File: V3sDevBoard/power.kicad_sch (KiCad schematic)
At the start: 48 parts, among them J10 Power, U2 SY8089AAAC, U3 SY8089AAAC, U4 SY8089AAAC, U6 PT4103

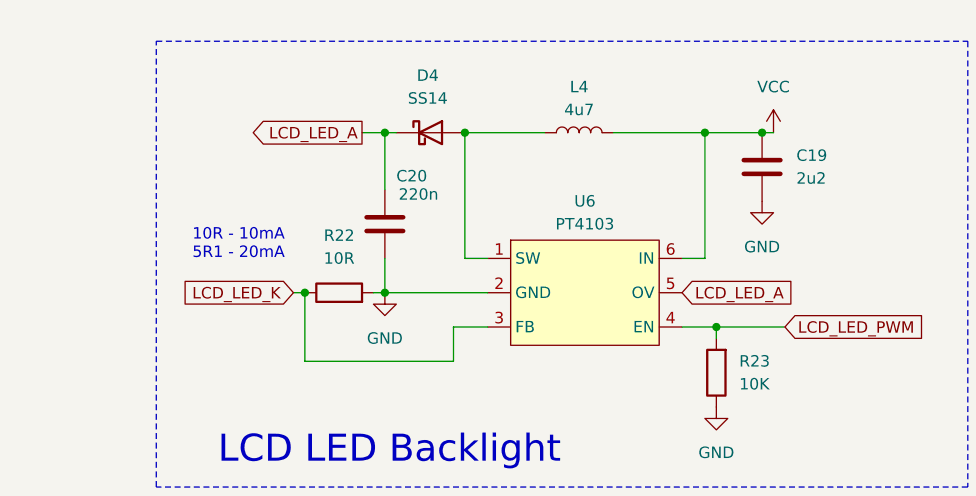
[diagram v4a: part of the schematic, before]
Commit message: first attempts to arrange components on a PCB
plus making footprints bme280&mpu6050 easier to hand solder.
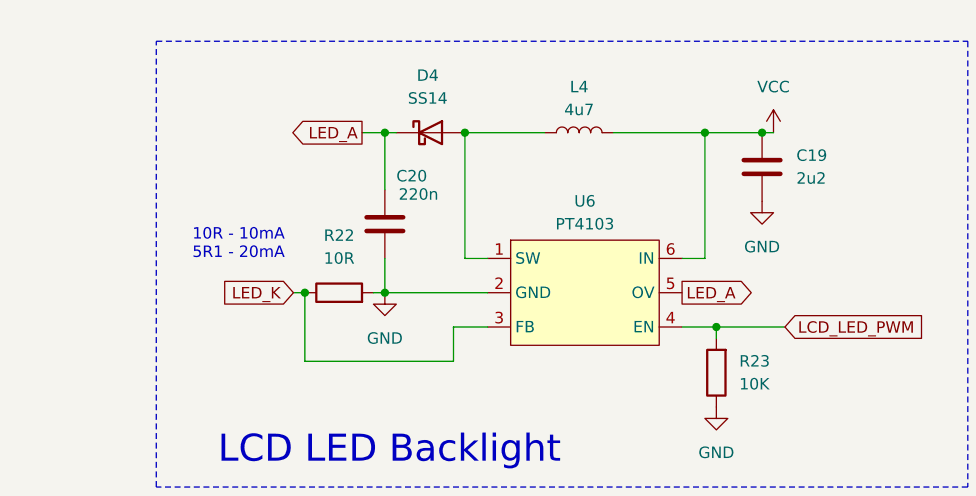
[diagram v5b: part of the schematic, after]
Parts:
- L1, L2, L3, L4: footprint Inductor_SMD:L_APV_APH0420 -> Inductor_SMD:L_APV_APH0420_HandSolder
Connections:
- net LCD_LED_A renamed LED_A
- net LCD_LED_K renamed LED_K
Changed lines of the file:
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@@
 		)
 	)
-	(global_label "LCD_LED_A"
+	(global_label "LED_A"
 		(shape output)
 		(at 194.31 27.94 180)
@@
 		)
 		(property "Intersheetrefs" "${INTERSHEET_REFS}"
-			(at 181.2858 27.94 0)
+			(at 185.8215 27.94 0)
 			(effects
 				(font
@@
 		)
 	)
-	(global_label "RGB"
-		(shape input)
-		(at 175.26 92.71 180)
+	(global_label "LED_A"
+		(shape output)
+		(at 229.87 45.72 0)
 		(fields_autoplaced yes)
 		(effects
@@
 				(size 1.27 1.27)
 			)
-			(justify right)
+			(justify left)
 		)
 		(property "Intersheetrefs" "${INTERSHEET_REFS}"
-			(at 168.4648 92.71 0)
+			(at 238.3585 45.72 0)
 			(effects
 				(font
 					(size 1.27 1.27)
 				)
-				(justify right)
+				(justify left)
 				(hide yes)
 			)
 		)
 	)
-	(global_label "LCD_LED_A"
+	(global_label "RGB"
 		(shape input)
-		(at 229.87 45.72 0)
+		(at 175.26 92.71 180)
 		(fields_autoplaced yes)
 		(effects
@@
 				(size 1.27 1.27)
 			)
-			(justify left)
+			(justify right)
 		)
 		(property "Intersheetrefs" "${INTERSHEET_REFS}"
-			(at 242.8942 45.72 0)
+			(at 168.4648 92.71 0)
 			(effects
 				(font
 					(size 1.27 1.27)
 				)
-				(justify left)
+				(justify right)
 				(hide yes)
 			)
 		)
 	)
-	(global_label "LCD_LED_K"
+	(global_label "LED_K"
 		(shape input)
 		(at 186.69 45.72 180)
@@
 		)
 		(property "Intersheetrefs" "${INTERSHEET_REFS}"
-			(at 173.4844 45.72 0)
+			(at 178.0201 45.72 0)
 			(effects
 				(font
@@
 		)
 	)
+	(rule_area
+		(polyline
+			(pts
+				(xy 36.83 21.59) (xy 36.83 58.42) (xy 39.37 60.96) (xy 73.66 60.96) (xy 73.66 69.85) (xy 119.38 69.85)
+				(xy 119.38 69.215) (xy 119.38 39.37) (xy 92.71 39.37) (xy 91.44 40.64) (xy 91.44 17.78) (xy 40.64 17.78)
+			)
+			(stroke
+				(width 0)
+				(type dash)
+			)
+			(fill
+				(type none)
+			)
+		)
+	)
+	(rule_area
+		(polyline
+			(pts
+				(xy 35.56 71.12) (xy 35.56 105.41) (xy 36.83 106.68) (xy 74.93 106.68) (xy 74.93 118.11) (xy 77.47 120.65)
+				(xy 127 120.65) (xy 127 88.9) (xy 124.46 86.36) (xy 92.71 86.36) (xy 90.17 83.82) (xy 90.17 76.2)
+				(xy 76.2 76.2) (xy 71.12 71.12) (xy 71.12 64.77) (xy 41.91 64.77)
+			)
+			(stroke
+				(width 0)
+				(type dash)
+			)
+			(fill
+				(type none)
+			)
+		)
+	)
+	(rule_area
+		(polyline
+			(pts
+				(xy 35.56 119.38) (xy 35.56 154.94) (xy 49.53 168.91) (xy 127 168.91) (xy 128.27 167.64) (xy 128.27 133.35)
+				(xy 119.38 124.46) (xy 76.2 124.46) (xy 72.39 120.65) (xy 72.39 114.3) (xy 40.64 114.3)
+			)
+			(stroke
+				(width 0)
+				(type dash)
+			)
+			(fill
+				(type none)
+			)
+		)
+	)
 	(netclass_flag ""
 		(length 2.54)
@@
 		(length 2.54)
 		(shape round)
+		(at 119.38 39.37 0)
+		(fields_autoplaced yes)
+		(effects
+			(font
+				(size 1.27 1.27)
+			)
+			(justify left bottom)
+		)
+		(property "Netclass" ""
+			(at 120.0785 36.83 0)
+			(effects
+				(font
+					(size 1.27 1.27)
+				)
+				(justify left)
+			)
+		)
+		(property "Component Class" "3V3 Power"
+			(at 120.0785 36.83 0)
+			(effects
+				(font
+					(size 1.27 1.27)
+					(italic yes)
+				)
+				(justify left)
+			)
+		)
+	)
+	(netclass_flag ""
+		(length 2.54)
+		(shape round)
 		(at 115.57 99.06 0)
 		(effects
@@
 		(length 2.54)
 		(shape round)
+		(at 120.65 86.36 0)
+		(fields_autoplaced yes)
+		(effects
+			(font
+				(size 1.27 1.27)
+			)
+			(justify left bottom)
+		)
+		(property "Netclass" ""
+			(at 121.3485 83.82 0)
+			(effects
+				(font
+					(size 1.27 1.27)
+				)
+				(justify left)
+			)
+		)
+		(property "Component Class" "1V8 Power"
+			(at 121.3485 83.82 0)
+			(effects
+				(font
+					(size 1.27 1.27)
+					(italic yes)
+				)
+				(justify left)
+			)
+		)
+	)
+	(netclass_flag ""
+		(length 2.54)
+		(shape round)
+		(at 128.27 133.35 0)
+		(fields_autoplaced yes)
+		(effects
+			(font
+				(size 1.27 1.27)
+			)
+			(justify left bottom)
+		)
+		(property "Netclass" ""
+			(at 128.9685 130.81 0)
+			(effects
+				(font
+					(size 1.27 1.27)
+				)
+				(justify left)
+			)
+		)
+		(property "Component Class" "1V2 Power"
+			(at 128.9685 130.81 0)
+			(effects
+				(font
+					(size 1.27 1.27)
+					(italic yes)
+				)
+				(justify left)
+			)
+		)
+	)
+	(netclass_flag ""
+		(length 2.54)
+		(shape round)
 		(at 67.31 22.86 90)
 		(effects
@@
 			)
 		)
-		(property "Footprint" "Inductor_SMD:L_APV_APH0420"
+		(property "Footprint" "Inductor_SMD:L_APV_APH0420_HandSolder"
 			(at 218.44 27.94 0)
 			(effects
@@
 			)
 		)
-		(property "Footprint" "Inductor_SMD:L_APV_APH0420"
+		(property "Footprint" "Inductor_SMD:L_APV_APH0420_HandSolder"
 			(at 86.36 148.59 0)
 			(effects
@@
 			)
 		)
-		(property "Footprint" "Inductor_SMD:L_APV_APH0420"
+		(property "Footprint" "Inductor_SMD:L_APV_APH0420_HandSolder"
 			(at 86.36 49.53 0)
 			(effects
@@
 			)
 		)
-		(property "Footprint" "Inductor_SMD:L_APV_APH0420"
+		(property "Footprint" "Inductor_SMD:L_APV_APH0420_HandSolder"
 			(at 86.36 99.06 0)
 			(effects

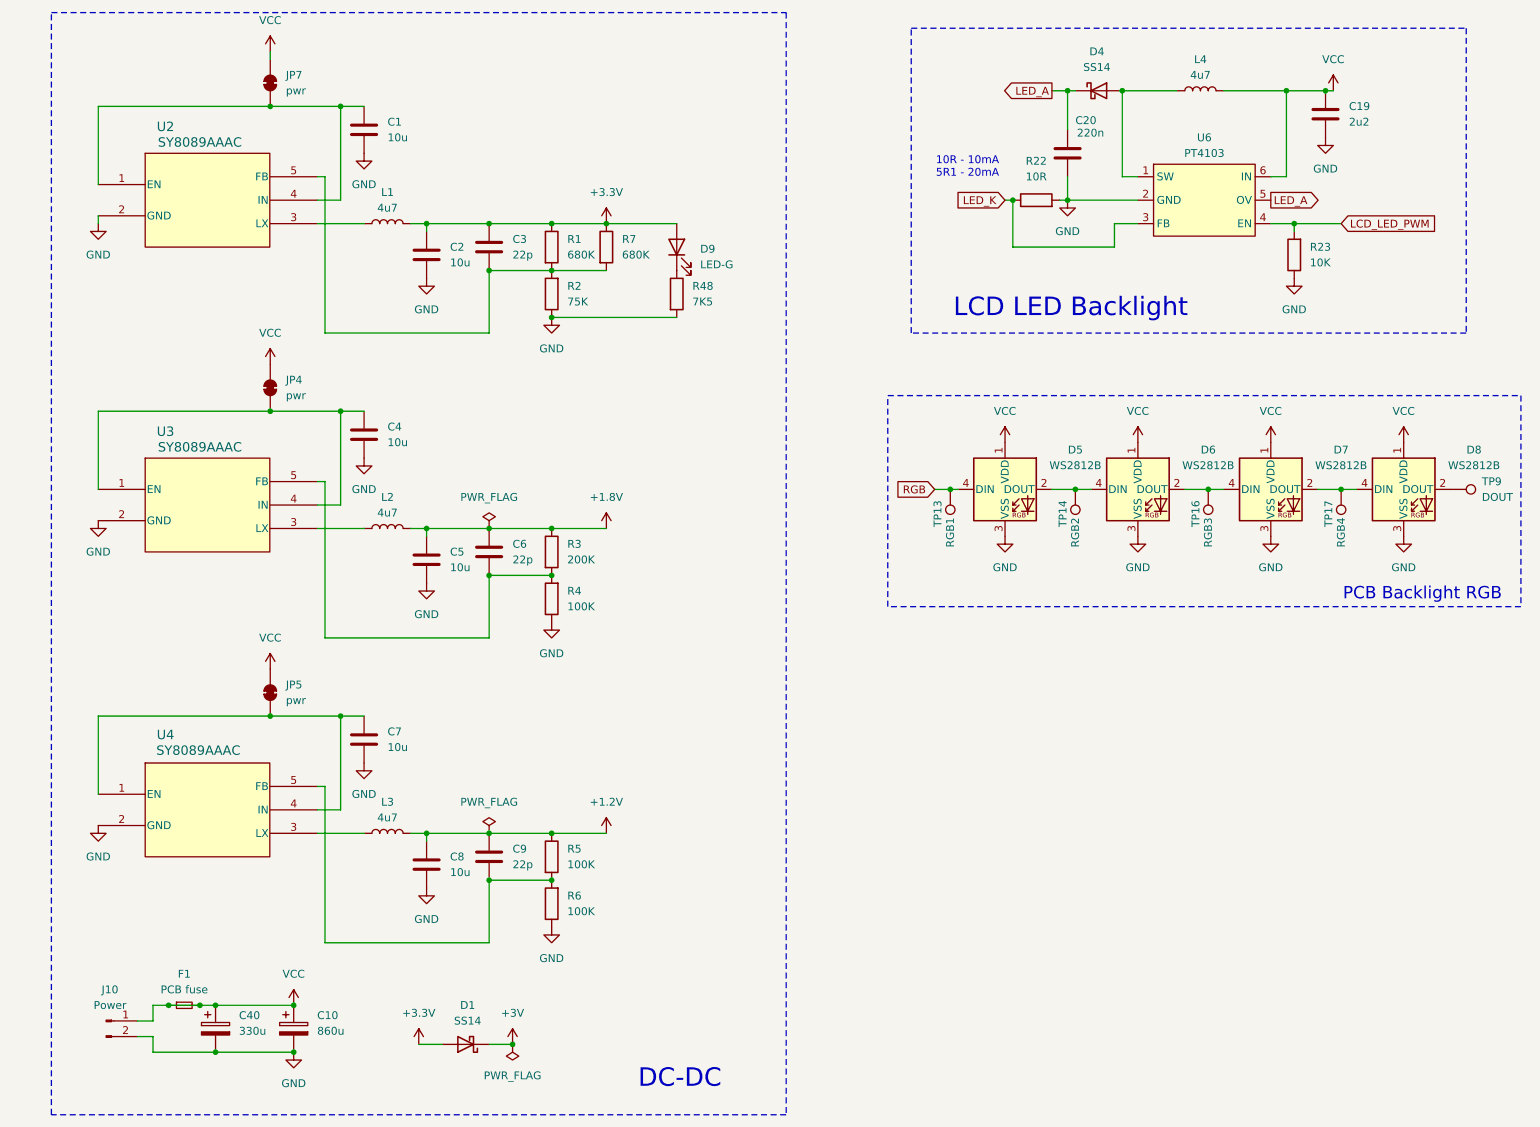
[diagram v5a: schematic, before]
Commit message: completing pcb desgin
Returning to project after month away. Switching to 4-layer desgin on 3313 stackup sig-gnd-pow-sig, changing size of some passive to 0603, connecting all components, adding silkscreen.
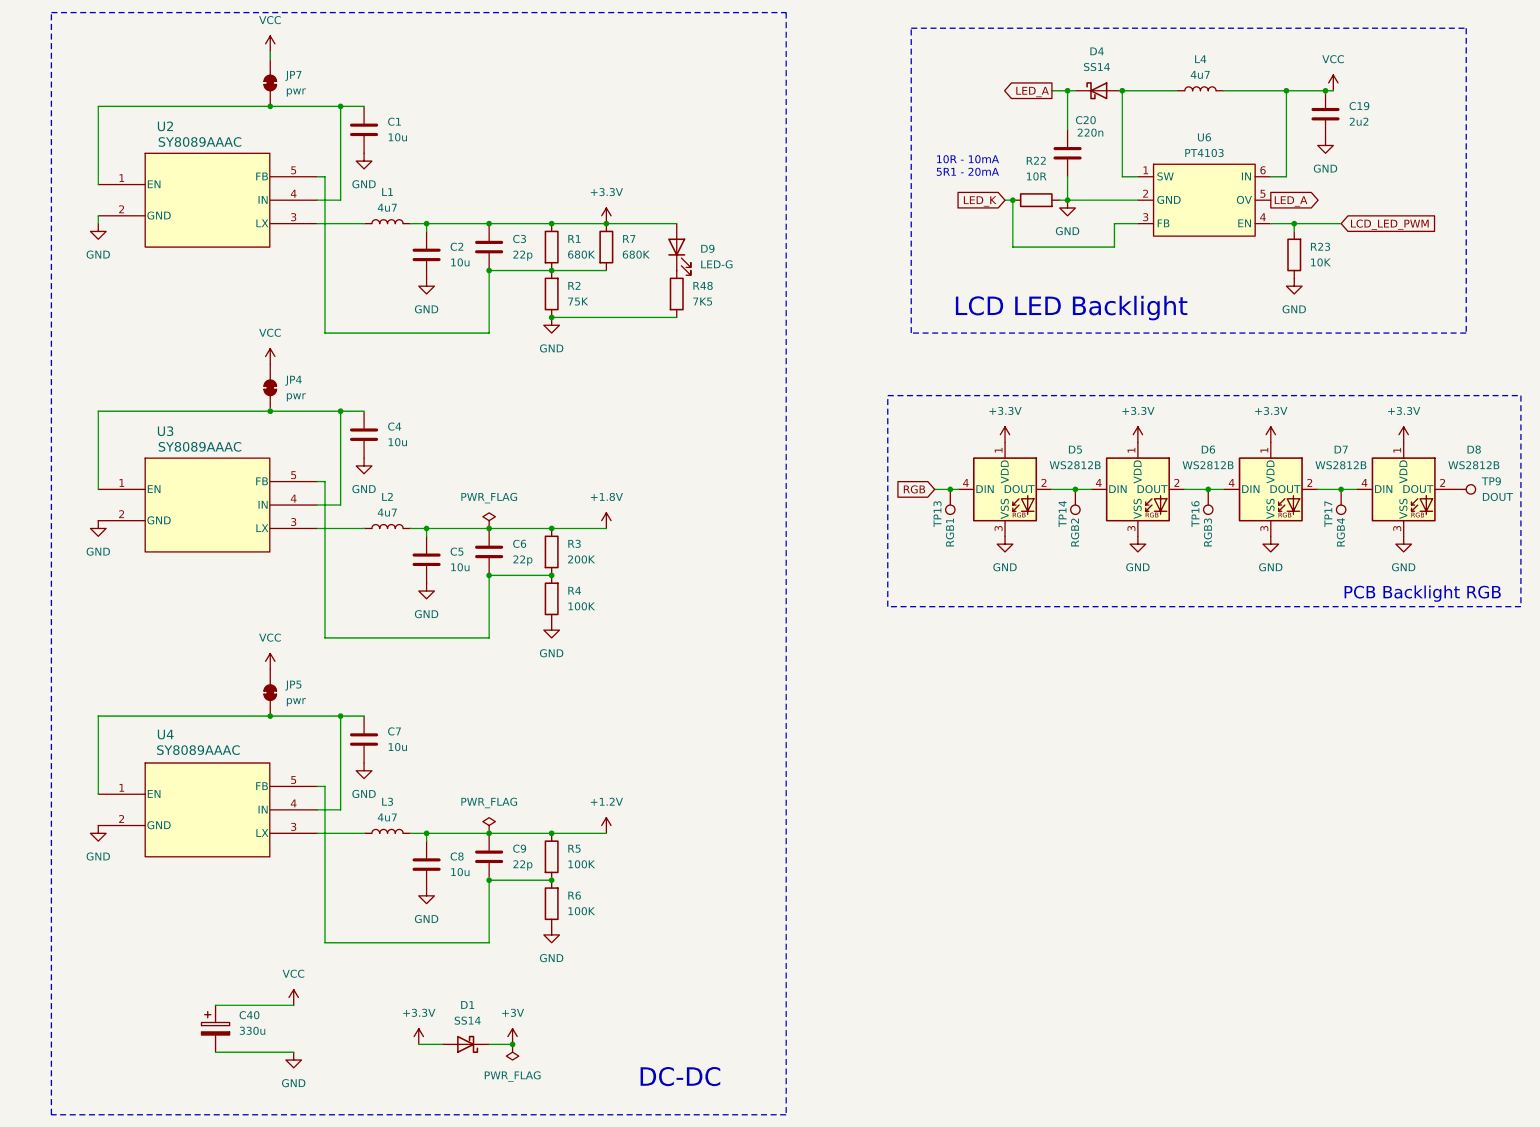
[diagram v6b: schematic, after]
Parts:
- removed C10: 860u, Capacitor_THT:CP_Radial_D6.3mm_P2.50mm, symbol Device:C_Polarized
- removed F1: PCB fuse, Fuse:Fuse_1206_3216Metric, symbol Device:Fuse_Small
- removed J10: Power, Connector_PinHeader_2.54mm:PinHeader_1x02_P2.54mm_Vertical, symbol Connector:Conn_01x02_Pin
- R1, R2, R23, R3, R4, R48, R5, R6: footprint Resistor_SMD:R_0805_2012Metric_Pad1.20x1.40mm_HandSolder -> Resistor_SMD:R_0603_1608Metric_Pad0.98x0.95mm_HandSolder
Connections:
- net +3.3V: now also D5.1 (VDD), D6.1 (VDD), D7.1 (VDD), D8.1 (VDD)
- net VCC: no longer D5.1 (VDD), D6.1 (VDD), D7.1 (VDD), D8.1 (VDD)
